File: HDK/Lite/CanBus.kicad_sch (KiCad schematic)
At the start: 10 parts, among them J201 TERM, U201 SN65HVD230, U202 MCP2518FD, Y201 40MHz

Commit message: updated 1 Job, WIP
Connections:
- net OSC_IN: now also C203.1, Y201.1; no longer C204.1, Y201.4
- net OSC_OUT: now also C204.1, Y201.4; no longer C203.1, Y201.1
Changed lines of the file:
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@@
     (effects (font (size 1.27 1.27)) (justify left bottom))
   )
-  (label "OSC_OUT" (at 68.58 87.63 0) (fields_autoplaced)
-    (effects (font (size 1.27 1.27)) (justify left bottom))
+  (label "OSC_OUT" (at 93.98 87.63 180) (fields_autoplaced)
+    (effects (font (size 1.27 1.27)) (justify right bottom))
   )
   (label "OSC_IN" (at 110.49 97.79 0) (fields_autoplaced)
     (effects (font (size 1.27 1.27)) (justify left bottom))
   )
-  (label "OSC_IN" (at 93.98 87.63 180) (fields_autoplaced)
-    (effects (font (size 1.27 1.27)) (justify right bottom))
+  (label "OSC_IN" (at 68.58 87.63 0) (fields_autoplaced)
+    (effects (font (size 1.27 1.27)) (justify left bottom))
   )
   (label "SPI_CANCS" (at 110.49 87.63 0) (fields_autoplaced)

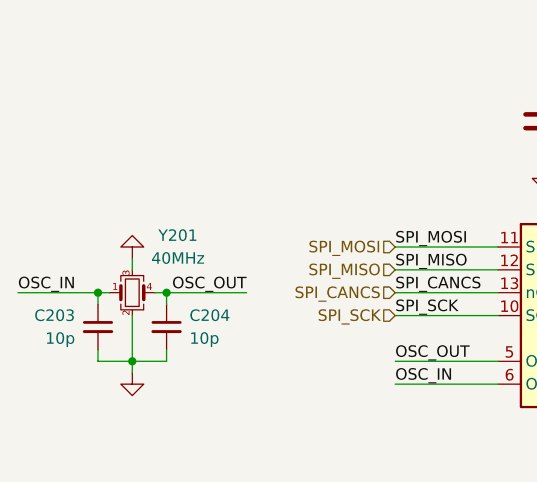
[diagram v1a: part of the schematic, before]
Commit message: updated 1Job, 75%
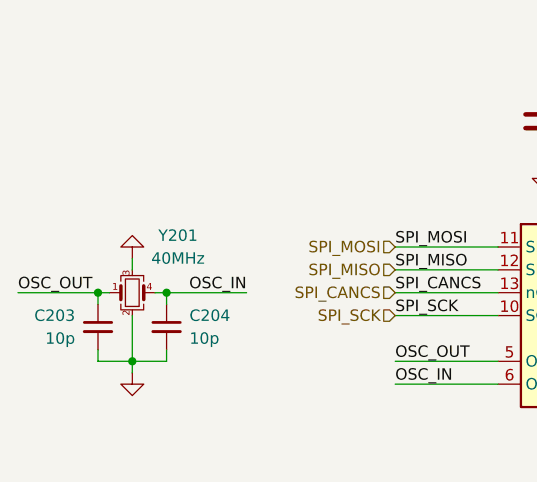
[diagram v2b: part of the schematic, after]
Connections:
- net OSC_IN: now also C204.1, Y201.4; no longer C203.1, Y201.1
- net OSC_OUT: now also C203.1, Y201.1; no longer C204.1, Y201.4
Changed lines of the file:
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@@
     (effects (font (size 1.27 1.27)) (justify left bottom))
   )
-  (label "OSC_OUT" (at 93.98 87.63 180) (fields_autoplaced)
-    (effects (font (size 1.27 1.27)) (justify right bottom))
+  (label "OSC_OUT" (at 68.58 87.63 0) (fields_autoplaced)
+    (effects (font (size 1.27 1.27)) (justify left bottom))
   )
   (label "OSC_IN" (at 110.49 97.79 0) (fields_autoplaced)
     (effects (font (size 1.27 1.27)) (justify left bottom))
   )
-  (label "OSC_IN" (at 68.58 87.63 0) (fields_autoplaced)
-    (effects (font (size 1.27 1.27)) (justify left bottom))
+  (label "OSC_IN" (at 93.98 87.63 180) (fields_autoplaced)
+    (effects (font (size 1.27 1.27)) (justify right bottom))
   )
   (label "SPI_CANCS" (at 110.49 87.63 0) (fields_autoplaced)
